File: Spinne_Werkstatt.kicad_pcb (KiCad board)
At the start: 2 copper layers, 15 parts, among them J1 Conn_01x02_Pin, J3 Conn_01x03_Pin, Q1 BSS138, Q2 BSS138, U2 CH340C, U4 ESP32-WROOM-32

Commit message: finished first pcb -- ugly
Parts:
- removed U4: ESP32-WROOM-32, bulme_footprints:ESP32-WROOM-32D
- added U1: ESP32-WROOM-32UE, RF_Module:ESP32-WROOM-32UE, F.Cu at (139.2, 62.8)
- esp_left1, esp_right1: value Conn_01x19_Pin -> Conn_01x15_Pin; footprint Connector_PinHeader_2.54mm:PinHeader_1x19_P2.54mm_Vertical -> Connector_PinHeader_2.54mm:PinHeader_1x15_P2.54mm_Vertical
- moved J1 20.1 mm to (132.7, 42.5), turned to 90 degrees
- moved D1 10.0 mm to (134.8, 49.8), turned to 0 degrees
- moved USB-C1 8.59 mm to (147.0, 49.8)
- moved Q1 4.25 mm to (152.8, 67.0)
- moved Q2 4.25 mm to (152.8, 71.5)
- moved C_USB_UART1 4.00 mm to (156.2, 51.2)
- moved U2 3.78 mm to (154.2, 58.8)
- moved J3 3.44 mm to (127.8, 42.5), turned to -90 degrees
- moved C_5V1 2.25 mm to (126.2, 49.0)
- moved esp_left1 2.10 mm to (131.0, 77.5)
- moved esp_right1 2.10 mm to (148.0, 77.5)
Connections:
- esp_left1 pad 15: pin15 -> pin16
- esp_right1 pad 10: pin29 -> pin28
- esp_right1 pad 11: pin28 -> pin27
- esp_right1 pad 12: pin27 -> pin26
- esp_right1 pad 13: pin26 -> ESP32_IO0
- esp_right1 pad 14: pin25 -> pin24
- esp_right1 pad 15: pin24 -> pin23
- esp_right1 pad 2: GND -> pin37
- esp_right1 pad 3: pin37 -> pin36
- esp_right1 pad 4: pin36 -> ESP32_TX
- esp_right1 pad 5: ESP32_TX -> ESP32_RX
- esp_right1 pad 6: ESP32_RX -> pin33
- esp_right1 pad 7: pin33 -> pin31
- esp_right1 pad 8: pin31 -> pin30
- esp_right1 pad 9: pin30 -> pin29
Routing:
- net GND: track 19.5 -> 164.2 mm, vias 0 -> 1
- net +3V3: track 0.00 -> 86.5 mm, vias 0 -> 1
- net ESP32_EN: track 0.00 -> 80.3 mm, vias 0 -> 3
- net +5V: track 30.1 -> 99.3 mm
- net pin12: track 0.00 -> 52.1 mm, vias 0 -> 1
- net pin27: track 0.00 -> 49.7 mm, vias 0 -> 2
- net pin23: track 0.00 -> 48.7 mm
- net pin11: track 0.00 -> 48.7 mm, vias 0 -> 1
- net ESP32_IO0: track 0.00 -> 47.8 mm
- net pin14: track 0.00 -> 47.0 mm
- net pin16: track 0.00 -> 46.9 mm
- net pin13: track 0.00 -> 46.6 mm
- net pin10: track 0.00 -> 46.5 mm, vias 0 -> 1
- net pin26: track 0.00 -> 46.0 mm, vias 0 -> 2
- net pin24: track 0.00 -> 45.6 mm
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- added copper zone on B.Cu, net GND
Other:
- board outline added: 42 x 79.2 mm

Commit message: nearly finished, not perfect but ok
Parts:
- removed C3: 1uF, Capacitor_SMD:C_0805_2012Metric_Pad1.18x1.45mm_HandSolder
- added C_ESP1: 22uF, Capacitor_SMD:CP_Elec_5x5.7, F.Cu at (123.2, 59.2)
- added C_ESP2: 100nF, Capacitor_SMD:C_0805_2012Metric_Pad1.18x1.45mm_HandSolder, F.Cu at (128.0, 58.0)
- added ESP_EN_R1: 10k, Resistor_SMD:R_1206_3216Metric_Pad1.30x1.75mm_HandSolder, F.Cu at (124.0, 51.2)
- D1: value D_Schottky -> ESDAULC6-3BP6; footprint Diode_SMD:D_1206_3216Metric_Pad1.42x1.75mm_HandSolder -> bulme_footprints:ESDAULC63BP6
- moved C_3.3V1 25.5 mm to (125.2, 44.0), turned to 90 degrees
- moved D1 17.1 mm to (151.8, 47.6), turned to 90 degrees
- moved Spannungsregler1 16.6 mm to (134.0, 47.2)
- moved C_5V1 16.5 mm to (142.5, 46.2), turned to -90 degrees
- moved J3 16.2 mm to (143.8, 39.8)
- moved USB-C1 10.4 mm to (154.7, 42.8)
- moved J1 2.94 mm to (133.8, 39.8), turned to -90 degrees
- moved C_USB_UART1 2.06 mm to (156.8, 53.2)
- moved Q2 1.94 mm to (154.1, 72.9)
- moved Q1 1.90 mm to (154.0, 68.4)
- moved U2 1.50 mm to (154.2, 60.2)
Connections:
- net ESP32_RX renamed ESP_RX
- net ESP32_TX renamed ESP_TX
- D1 pad 1: VBUS -> D+
- D1 pad 2: Net-(D1-A) -> (no net)
- USB-C1 pad A4: Net-(D1-A) -> VBUS
- USB-C1 pad A9: Net-(D1-A) -> VBUS
- USB-C1 pad B4: Net-(D1-A) -> VBUS
- USB-C1 pad B9: Net-(D1-A) -> VBUS
- esp_left1 pad 2: +3.3V -> +3V3
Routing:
- net GND: track 164.2 -> 5.86 mm, vias 1 -> 0
- net +5V: track 99.3 -> 20.7 mm
- net pin9: track 42.9 -> 0.00 mm, vias 1 -> 0
- net pin8: track 39.8 -> 0.00 mm, vias 1 -> 0
- net pin7: track 38.4 -> 0.00 mm, vias 1 -> 0
- net pin5: track 36.6 -> 0.00 mm, vias 2 -> 0
- net pin6: track 33.3 -> 0.00 mm, vias 1 -> 0
- net pin4: track 29.6 -> 0.00 mm
- net ESP32_EN: track 80.3 -> 55.3 mm, vias 3 -> 2
- net +3V3: track 86.5 -> 63.4 mm, vias 1 -> 2
- net Net-(D1-A): track 16.5 -> 0.00 mm
- net ESP_TX: track 21.2 -> 36.3 mm, vias 0 -> 1
- net D+: track 20.0 -> 32.7 mm, vias 1 -> 2
- net VBUS: track 10.6 -> 21.2 mm
- net D-: track 21.3 -> 31.4 mm
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- added copper zone on F.Cu, net GND
- removed copper zone on B.Cu, net GND
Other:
- board size 42 x 79.2 mm -> 42 x 81.2 mm

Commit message: finished, not that bad
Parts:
- moved C_ESP2 0.50 mm to (127.5, 58.0)
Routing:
- net pin9: track 0.00 -> 41.6 mm, vias 0 -> 1
- net pin4: track 0.00 -> 40.2 mm, vias 0 -> 2
- net pin8: track 0.00 -> 39.2 mm, vias 0 -> 1
- net pin7: track 0.00 -> 36.4 mm, vias 0 -> 1
- net +5V: track 20.7 -> 56.4 mm, vias 0 -> 1
- net pin6: track 0.00 -> 33.9 mm, vias 0 -> 1
- net ESP32_EN: track 55.3 -> 87.2 mm, vias 2 -> 4
- net pin5: track 0.00 -> 31.3 mm, vias 0 -> 1
- net +3V3: track 63.4 -> 94.6 mm, vias 2 -> 4
- net pin14: track 44.2 -> 53.5 mm, vias 0 -> 1
- net pin13: track 42.2 -> 50.2 mm, vias 0 -> 1
- net GND: track 5.86 -> 9.11 mm

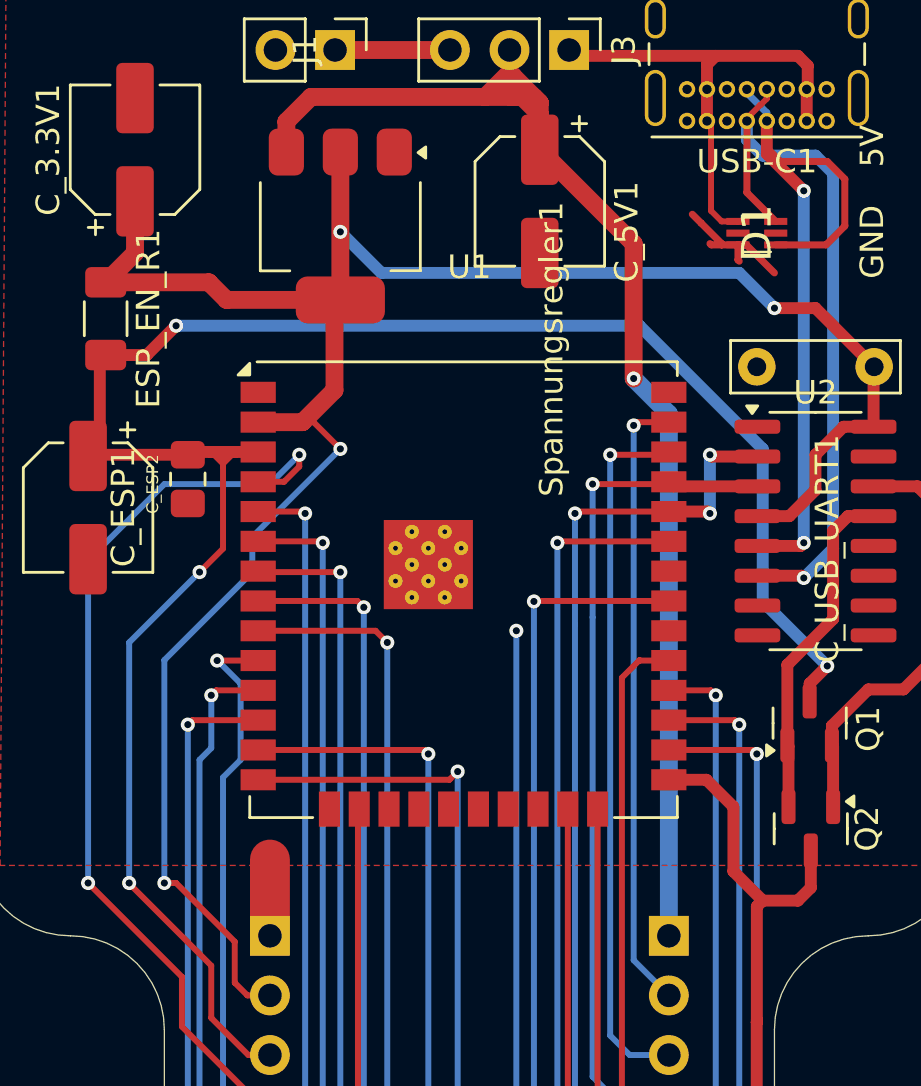
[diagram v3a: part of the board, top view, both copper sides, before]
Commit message: removed errors, only esp gnd and usb c port ramaining errors, not fixable
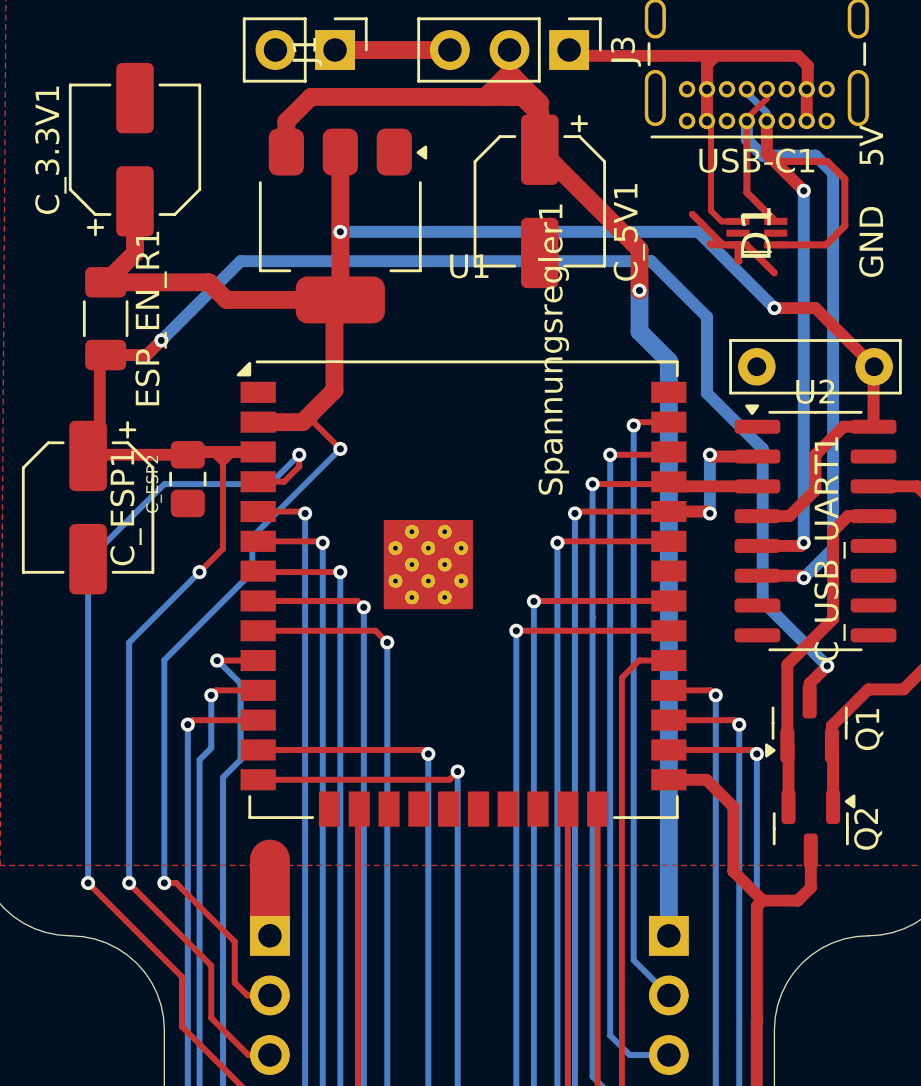
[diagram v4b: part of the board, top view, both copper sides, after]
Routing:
- net pin30: track 34.3 -> 40.8 mm
- net ESP32_EN: track 87.2 -> 91.3 mm

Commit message: added gerber
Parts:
- removed Spannungsregler1: AMS1117-3.3, Package_TO_SOT_SMD:SOT-223-3_TabPin2
- added AMS1117: AMS1117-3.3, Package_TO_SOT_SMD:SOT-223-3_TabPin2, F.Cu at (134.1, 46.9)
- moved D1 1.07 mm to (151.9, 46.5)
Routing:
- net D+: track 32.7 -> 24.7 mm
- net ESP32_EN: track 91.3 -> 94.1 mm
- net GND: track 9.11 -> 11.8 mm
- net VBUS: track 21.2 -> 19.6 mm
- net +3V3: track 94.6 -> 96.1 mm
- net ESP32_IO0: track 46.3 -> 47.6 mm
- net pin10: track 39.0 -> 37.9 mm, vias 2 -> 1
- net pin26: track 42.4 -> 41.3 mm
- net pin13: track 50.2 -> 51.1 mm
- net pin11: track 40.1 -> 39.4 mm, vias 2 -> 1
- net D-: track 31.4 -> 30.9 mm
- net pin12: track 42.4 -> 42.6 mm, vias 2 -> 1
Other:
- board size 42 x 81.2 mm -> 42 x 82 mm
- board text added: "EXT"
- board text added: "USB"
